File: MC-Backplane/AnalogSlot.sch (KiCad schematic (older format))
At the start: 1 part, among them U5 86094328314755V1LF

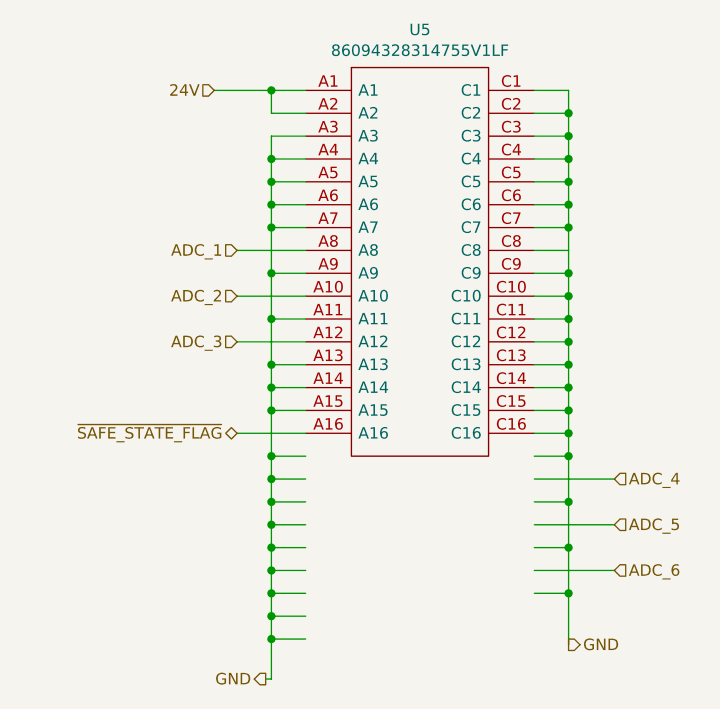
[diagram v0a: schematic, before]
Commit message: layout done: cleaning up and checking MH
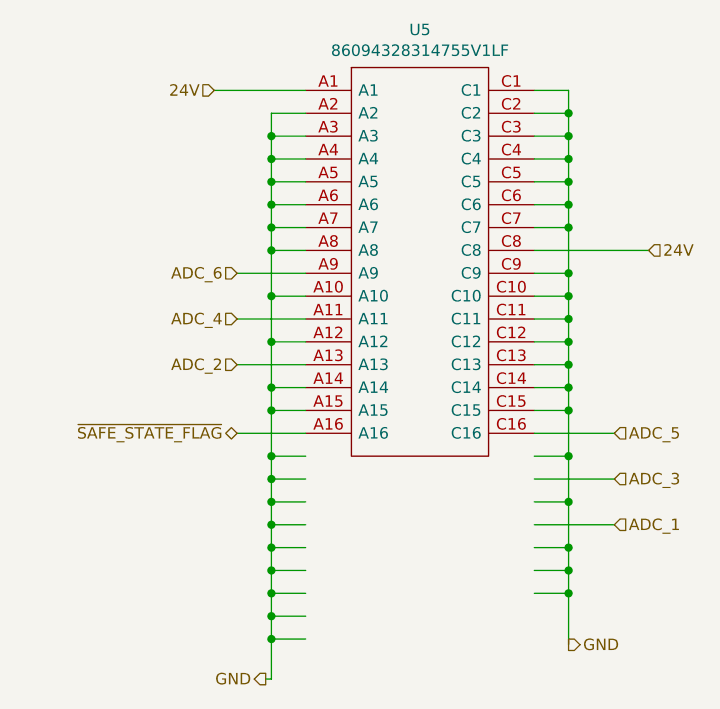
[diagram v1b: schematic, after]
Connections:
- wire segments 90 -> 89
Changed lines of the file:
@@
 	6225 4800 6375 4800
-Wire Wire Line
-	6375 3300 6225 3300
 Wire Wire Line
 	6375 3700 6225 3700
@@
 24V
 Wire Wire Line
-	5225 2600 5075 2600
-Wire Wire Line
 	5075 4000 5075 3900
 Connection ~ 5075 4000
 Wire Wire Line
 	5225 4000 5075 4000
-Wire Wire Line
-	5075 3900 5075 3800
 Connection ~ 5075 3900
 Wire Wire Line
 	5225 3900 5075 3900
-Wire Wire Line
-	5225 3800 5075 3800
-Wire Wire Line
-	5225 3600 5075 3600
-Wire Wire Line
-	5075 3400 5225 3400
 Wire Wire Line
 	5075 3200 5075 3100
@@
 Wire Wire Line
 	5225 2800 5075 2800
-Wire Wire Line
-	5075 2700 5225 2700
 Connection ~ 6375 4800
 Wire Wire Line
@@
 Text HLabel 5050 5175 0    50   Output ~ 0
 GND
-Text HLabel 6575 4500 2    50   Input ~ 0
+Text HLabel 6575 4100 2    50   Input ~ 0
 ADC_5
-Text HLabel 6575 4700 2    50   Input ~ 0
+Text HLabel 4925 3400 0    50   Input ~ 0
 ADC_6
 Wire Wire Line
@@
 Connection ~ 6375 4000
 Wire Wire Line
-	6375 4000 6375 4100
-Wire Wire Line
-	6375 4100 6225 4100
-Wire Wire Line
 	6575 4300 6225 4300
 Wire Wire Line
 	6575 4500 6225 4500
-Text HLabel 6575 4300 2    50   Input ~ 0
+Text HLabel 4925 3600 0    50   Input ~ 0
 ADC_4
 Wire Wire Line
@@
 Connection ~ 6375 3400
 Wire Wire Line
-	6225 4700 6575 4700
+	6225 4100 6575 4100
 Wire Wire Line
 	6225 4200 6375 4200
@@
 	6225 4600 6375 4600
 Connection ~ 6375 4600
-Wire Wire Line
-	6375 4600 6375 4800
-Text HLabel 4925 3700 0    50   Input ~ 0
+Text HLabel 6575 4300 2    50   Input ~ 0
 ADC_3
-Text HLabel 4925 3500 0    50   Input ~ 0
-ADC_2
-Text HLabel 4925 3300 0    50   Input ~ 0
+Text HLabel 6575 4500 2    50   Input ~ 0
 ADC_1
 Connection ~ 6375 3700
@@
 Wire Wire Line
 	6375 3900 6375 4000
-Connection ~ 6375 4100
-Wire Wire Line
-	6375 4100 6375 4200
-Wire Wire Line
-	4925 3300 5225 3300
-Wire Wire Line
-	4925 3500 5225 3500
-Wire Wire Line
-	4925 3700 5225 3700
-Wire Wire Line
-	5075 3400 5075 3600
-Connection ~ 5075 3800
-Connection ~ 5075 3600
-Wire Wire Line
-	5075 3600 5075 3800
-Wire Wire Line
-	5075 3200 5075 3400
+Wire Wire Line
+	4925 3400 5225 3400
+Wire Wire Line
+	4925 3600 5225 3600
 Connection ~ 5075 3200
-Connection ~ 5075 3400
 Wire Wire Line
 	6375 3400 6375 3500
@@
 Wire Wire Line
 	6375 3600 6225 3600
-Wire Wire Line
-	5075 2700 5075 2600
-Connection ~ 5075 2600
-Wire Wire Line
-	5075 2600 4825 2600
 $Comp
 L Existing_IC_Models:86094328314755V1LF U?
@@
 Wire Wire Line
 	5075 4900 5075 5000
+Wire Wire Line
+	4925 3800 5225 3800
+Text HLabel 4925 3800 0    50   Input ~ 0
+ADC_2
+Wire Wire Line
+	5225 3700 5075 3700
+Connection ~ 5075 3700
+Wire Wire Line
+	5075 3700 5075 3900
+Wire Wire Line
+	5225 3500 5075 3500
+Connection ~ 5075 3500
+Wire Wire Line
+	5075 3500 5075 3700
+Wire Wire Line
+	6375 4000 6375 4200
+Wire Wire Line
+	6225 4700 6375 4700
+Wire Wire Line
+	6375 4600 6375 4700
+Connection ~ 6375 4700
+Wire Wire Line
+	6375 4700 6375 4800
+Wire Wire Line
+	5075 3200 5075 3300
+Wire Wire Line
+	5225 3300 5075 3300
+Connection ~ 5075 3300
+Wire Wire Line
+	5075 3300 5075 3500
+Wire Wire Line
+	4825 2600 5225 2600
+Wire Wire Line
+	6225 3300 6725 3300
+Text HLabel 6725 3300 2    50   Input ~ 0
+24V
+Wire Wire Line
+	5225 2700 5075 2700
+Wire Wire Line
+	5075 2700 5075 2800
+Connection ~ 5075 2800
 $EndSCHEMATC

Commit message: Layout ready for review
- double check measurements and connector placement
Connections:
- wire segments 89 -> 56
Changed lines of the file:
@@
 $Descr A4 11693 8268
 encoding utf-8
-Sheet 5 14
+Sheet 10 14
 Title ""
 Date ""
@@
 Comment4 ""
 $EndDescr
-Text HLabel 6375 5025 2    50   Output ~ 0
+Text HLabel 6375 4400 2    50   Output ~ 0
 GND
 Wire Wire Line
-	6225 4800 6375 4800
+	6225 4100 6375 4100
 Wire Wire Line
-	6375 3700 6225 3700
+	6375 3000 6225 3000
 Wire Wire Line
-	6225 3900 6375 3900
+	6225 3200 6375 3200
 Text HLabel 4825 2600 0    50   Input ~ 0
 24V
@@
 Wire Wire Line
 	5225 2800 5075 2800
-Connection ~ 6375 4800
+Connection ~ 6375 4100
 Wire Wire Line
-	6375 4800 6375 5025
+	6375 4100 6375 4400
 Wire Wire Line
-	6375 3800 6225 3800
+	6375 3100 6225 3100
 Wire Wire Line
-	6375 3800 6375 3700
-Connection ~ 6375 3800
+	6375 3100 6375 3000
+Connection ~ 6375 3100
 Wire Wire Line
-	6375 3400 6225 3400
-Text HLabel 5050 5175 0    50   Output ~ 0
+	6375 2700 6225 2700
+Text HLabel 5050 4400 0    50   Output ~ 0
 GND
-Text HLabel 6575 4100 2    50   Input ~ 0
+Text HLabel 6575 3400 2    50   Input ~ 0
 ADC_5
 Text HLabel 4925 3400 0    50   Input ~ 0
 ADC_6
 Wire Wire Line
-	6375 3800 6375 3900
+	6375 3100 6375 3200
 Wire Wire Line
-	6225 4000 6375 4000
-Connection ~ 6375 4000
+	6225 3300 6375 3300
+Connection ~ 6375 3300
 Wire Wire Line
-	6575 4300 6225 4300
+	6575 3600 6225 3600
 Wire Wire Line
-	6575 4500 6225 4500
+	6575 3800 6225 3800
 Text HLabel 4925 3600 0    50   Input ~ 0
 ADC_4
 Wire Wire Line
-	6375 3300 6375 3400
-Connection ~ 6375 3400
+	6225 3400 6575 3400
 Wire Wire Line
-	6225 4100 6575 4100
+	6225 3500 6375 3500
+Connection ~ 6375 3500
 Wire Wire Line
-	6225 4200 6375 4200
-Connection ~ 6375 4200
+	6375 3500 6375 3700
 Wire Wire Line
-	6375 4200 6375 4400
+	6225 3700 6375 3700
+Connection ~ 6375 3700
 Wire Wire Line
-	6225 4400 6375 4400
-Connection ~ 6375 4400
+	6375 3700 6375 3900
 Wire Wire Line
-	6375 4400 6375 4600
+	6225 3900 6375 3900
+Connection ~ 6375 3900
+Text HLabel 6575 3600 2    50   Input ~ 0
+ADC_3
+Text HLabel 6575 3800 2    50   Input ~ 0
+ADC_1
+Connection ~ 6375 3000
+Connection ~ 6375 3200
 Wire Wire Line
-	6225 4600 6375 4600
-Connection ~ 6375 4600
-Text HLabel 6575 4300 2    50   Input ~ 0
-ADC_3
-Text HLabel 6575 4500 2    50   Input ~ 0
-ADC_1
-Connection ~ 6375 3700
-Connection ~ 6375 3900
-Wire Wire Line
-	6375 3900 6375 4000
+	6375 3200 6375 3300
 Wire Wire Line
 	4925 3400 5225 3400
@@
 Connection ~ 5075 3200
 Wire Wire Line
-	6375 3400 6375 3500
+	6375 2700 6375 2800
 Wire Wire Line
-	6225 3500 6375 3500
-Connection ~ 6375 3500
+	6225 2800 6375 2800
+Connection ~ 6375 2800
 Wire Wire Line
-	6375 3500 6375 3600
+	6375 2800 6375 2900
 Wire Wire Line
-	6375 3600 6225 3600
+	6375 2900 6225 2900
 $Comp
 L Existing_IC_Models:86094328314755V1LF U?
@@
 AR Path="/62480E35/62372321" Ref="U10"  Part="1"
 AR Path="/6248CEED/62372321" Ref="U11"  Part="1"
-F 0 "U5" H 5725 2865 50  0000 C CNN
+F 0 "U10" H 5725 2865 50  0000 C CNN
 F 1 "86094328314755V1LF" H 5725 2774 50  0000 C CNN
 F 2 "Footprints_MC-Backplane:86094328314755V1LF" H 6075 2700 50  0001 L CNN
@@
 $EndComp
 Wire Wire Line
-	5225 4200 5075 4200
-Wire Wire Line
-	5075 4400 5225 4400
-Wire Wire Line
-	5225 4300 5075 4300
-Wire Wire Line
-	5075 4500 5225 4500
-Wire Wire Line
-	5225 4600 5075 4600
-Wire Wire Line
-	5075 4700 5225 4700
-Wire Wire Line
-	5225 5000 5075 5000
-Wire Wire Line
-	5225 4800 5075 4800
-Connection ~ 5075 4300
-Connection ~ 5075 4200
-Wire Wire Line
-	5075 4200 5075 4300
-Wire Wire Line
-	5075 4300 5075 4400
-Wire Wire Line
-	5075 4400 5075 4500
-Wire Wire Line
-	5075 5175 5050 5175
-Connection ~ 5075 4400
-Connection ~ 5075 4500
-Wire Wire Line
-	5075 4500 5075 4600
-Connection ~ 5075 4600
-Wire Wire Line
-	5075 4600 5075 4700
-Connection ~ 5075 4700
-Wire Wire Line
-	5075 4700 5075 4800
-Connection ~ 5075 4800
-Connection ~ 5075 5000
-Wire Wire Line
-	5075 5000 5075 5175
-Wire Wire Line
-	6225 2600 6375 2600
-Wire Wire Line
-	6375 2600 6375 2700
-Wire Wire Line
-	6225 2700 6375 2700
-Connection ~ 6375 2700
-Wire Wire Line
-	6375 2700 6375 2800
-Wire Wire Line
-	6375 2800 6225 2800
-Connection ~ 6375 2800
-Wire Wire Line
-	6375 2800 6375 2900
-Wire Wire Line
-	6225 2900 6375 2900
+	5075 4400 5050 4400
 Connection ~ 6375 2900
 Wire Wire Line
 	6375 2900 6375 3000
-Wire Wire Line
-	6375 3000 6225 3000
-Connection ~ 6375 3000
-Wire Wire Line
-	6375 3000 6375 3100
-Wire Wire Line
-	6375 3100 6225 3100
-Connection ~ 6375 3100
-Wire Wire Line
-	6375 3100 6375 3200
-Wire Wire Line
-	6225 3200 6375 3200
-Connection ~ 6375 3200
-Wire Wire Line
-	6375 3200 6375 3300
-Wire Wire Line
-	5075 4800 5075 4900
-Connection ~ 6375 3600
-Wire Wire Line
-	6375 3600 6375 3700
-Wire Wire Line
-	5225 4900 5075 4900
 Text HLabel 4925 4100 0    50   BiDi ~ 0
 ~SAFE_STATE_FLAG~
 Wire Wire Line
-	5075 4000 5075 4200
-Wire Wire Line
 	5225 4100 4925 4100
-Connection ~ 5075 4900
-Wire Wire Line
-	5075 4900 5075 5000
 Wire Wire Line
 	4925 3800 5225 3800
@@
 	5075 3500 5075 3700
 Wire Wire Line
-	6375 4000 6375 4200
+	6375 3300 6375 3500
 Wire Wire Line
-	6225 4700 6375 4700
+	6225 4000 6375 4000
 Wire Wire Line
-	6375 4600 6375 4700
-Connection ~ 6375 4700
+	6375 3900 6375 4000
+Connection ~ 6375 4000
 Wire Wire Line
-	6375 4700 6375 4800
+	6375 4000 6375 4100
 Wire Wire Line
 	5075 3200 5075 3300
@@
 Wire Wire Line
 	4825 2600 5225 2600
-Wire Wire Line
-	6225 3300 6725 3300
-Text HLabel 6725 3300 2    50   Input ~ 0
+Text HLabel 6725 2600 2    50   Input ~ 0
 24V
 Wire Wire Line
@@
 	5075 2700 5075 2800
 Connection ~ 5075 2800
+Wire Wire Line
+	5075 4000 5075 4400
+Wire Wire Line
+	6225 2600 6725 2600
 $EndSCHEMATC

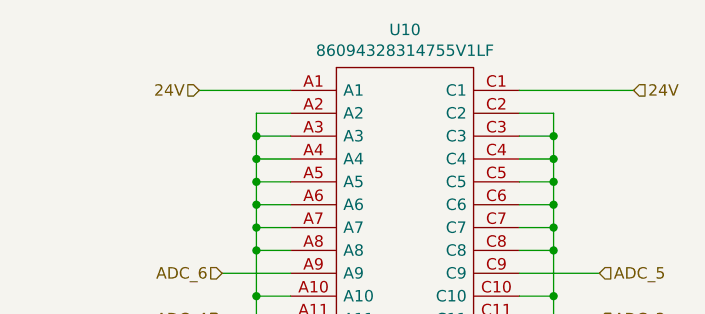
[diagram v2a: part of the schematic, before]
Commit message: added testpoints
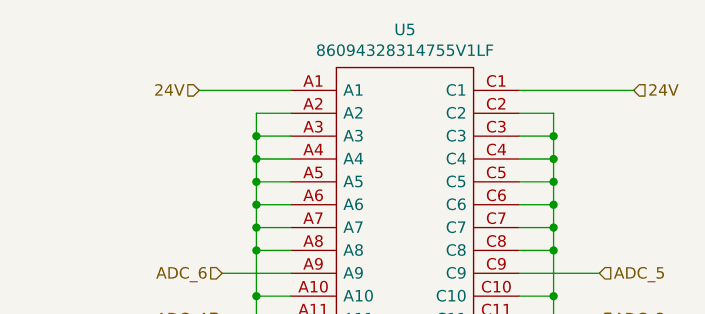
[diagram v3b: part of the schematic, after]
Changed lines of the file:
@@
 $Descr A4 11693 8268
 encoding utf-8
-Sheet 10 14
+Sheet 5 14
 Title ""
 Date ""
@@
 AR Path="/62480E35/62372321" Ref="U10"  Part="1"
 AR Path="/6248CEED/62372321" Ref="U11"  Part="1"
-F 0 "U10" H 5725 2865 50  0000 C CNN
+F 0 "U5" H 5725 2865 50  0000 C CNN
 F 1 "86094328314755V1LF" H 5725 2774 50  0000 C CNN
 F 2 "Footprints_MC-Backplane:86094328314755V1LF" H 6075 2700 50  0001 L CNN
